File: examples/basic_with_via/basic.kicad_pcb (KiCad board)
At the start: 2 copper layers, 9 x 14 mm, 7 parts

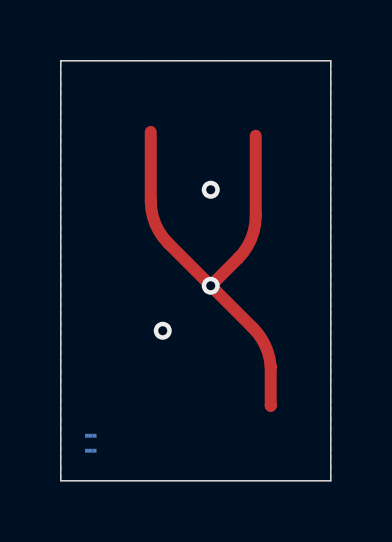
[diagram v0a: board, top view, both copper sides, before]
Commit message: add with via
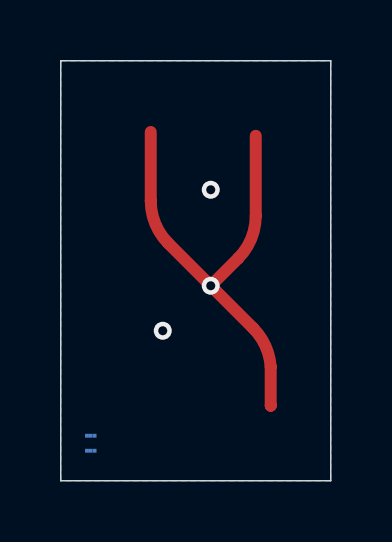
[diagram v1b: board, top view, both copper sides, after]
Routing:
- removed copper zone on F.Cu, net (none)
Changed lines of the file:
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@@
 			(drillshape 0)
 			(scaleselection 1)
-			(outputdirectory "fab/")
+			(outputdirectory "")
 		)
 	)
@@
 		)
 		(fp_text user "{REFERENCE}"
-			(at 0 3 180)
+			(at 0 3 0)
 			(layer "F.Fab")
 			(hide yes)
@@
 	)
 	(zone
-		(net 0)
-		(net_name "")
-		(layer "F.Cu")
-		(hatch edge 0.5)
-		(priority 1)
-		(connect_pads
-			(clearance 0.2)
-		)
-		(min_thickness 0.25)
-		(filled_areas_thickness no)
-		(fill yes
-			(thermal_gap 0.5)
-			(thermal_bridge_width 0.5)
-			(island_removal_mode 1)
-			(island_area_min 10)
-		)
-		(polygon
-			(pts
-				(xy 140 101) (xy 140 115) (xy 149 115) (xy 149 101)
-			)
-		)
-	)
-	(zone
